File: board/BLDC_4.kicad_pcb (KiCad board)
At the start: 2 copper layers, 100 x 80 mm, 53 parts, among them IC1 MAX3051, P1 Interface, P2 SWD, P3 USB_B, P4 Power, U1 STM32F40X_LQFP64, U2 AP1117D33, X2 8MHz 10ppm

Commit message: - preliminary layout for CPU board ready
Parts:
- removed C23: 1n, Capacitors_SMD:C_0805
- removed C35: 2.2u, Capacitors_SMD:C_0805
- C14: value 2.2u -> 100n
- C18: value 2u2 -> 1n
- moved REF** 390.6 mm to (176.0, 92.0)
- moved C31 106.0 mm to (252.6, 51.4), turned to 90 degrees
- moved C14 105.3 mm to (262.2, 60.0), turned to 180 degrees
- moved C13 83.2 mm to (234.4, 42.8), turned to 225 degrees
- moved C32 77.9 mm to (233.8, 64.2)
- moved C11 72.6 mm to (235.0, 57.0), turned to 180 degrees
- moved C10 68.9 mm to (216.4, 58.8)
- moved C12 66.7 mm to (219.6, 43.2), turned to 270 degrees
- moved C2 44.6 mm to (204.8, 49.2), turned to 180 degrees
- moved C1 30.7 mm to (200.6, 46.0), turned to 270 degrees
- moved C8 14.3 mm to (262.2, 62.0), turned to 0 degrees
- moved C19 10.6 mm to (262.2, 44.0)
- moved C20 8.40 mm to (262.2, 52.4)
- moved C21 5.40 mm to (258.8, 48.2), turned to 90 degrees
- moved C18 5.20 mm to (262.2, 54.8)
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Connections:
- C14 pad 1: GND -> /MCU/ADC_TEMP
- C14 pad 2: +3V3 -> GND
- C18 pad 1: /MCU/ADC_TEMP -> /MCU/BR_SO2
- C19 pad 1: /MCU/BR_SO2 -> /MCU/BR_SO1
- C20 pad 1: /MCU/BR_SO1 -> /MCU/SENS3
- C21 pad 1: /MCU/SENS3 -> /MCU/SENS2
- C22 pad 1: /MCU/SENS2 -> /MCU/SENS1
- P1 pad 18: Net-(P1-Pad18) -> (no net)
- P1 pad 19: Net-(P1-Pad19) -> (no net)
- P1 pad 20: Net-(P1-Pad20) -> (no net)
- P2 pad 6: Net-(P2-Pad6) -> (no net)
- P4 pad 30: Net-(P4-Pad30) -> (no net)
- P4 pad 32: Net-(P4-Pad32) -> (no net)
- P4 pad 34: Net-(P4-Pad34) -> (no net)
- P4 pad 36: Net-(P4-Pad36) -> (no net)
- P4 pad 40: +12V -> (no net)
- U1 pad 11: Net-(U1-Pad11) -> (no net)
- U1 pad 2: Net-(U1-Pad2) -> (no net)
- U1 pad 28: Net-(U1-Pad28) -> (no net)
- U1 pad 3: Net-(U1-Pad3) -> (no net)
- U1 pad 33: /MCU/DC_CAL -> (no net)
- U1 pad 39: Net-(U1-Pad39) -> (no net)
- U1 pad 4: Net-(U1-Pad4) -> (no net)
- U1 pad 40: Net-(U1-Pad40) -> (no net)
- U1 pad 50: Net-(U1-Pad50) -> (no net)
- U1 pad 53: /MCU/FAULT -> (no net)
- U1 pad 54: Net-(U1-Pad54) -> (no net)
- U1 pad 55: Net-(U1-Pad55) -> (no net)
- U1 pad 56: Net-(U1-Pad56) -> (no net)
- U1 pad 9: Net-(U1-Pad9) -> (no net)
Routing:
- net +3V3: track 14.8 -> 231.1 mm, vias 0 -> 5
- net GND: track 0.00 -> 47.9 mm, vias 0 -> 5
- net SWDIO: track 19.9 -> 25.6 mm
- net /MCU/AN_IN: track 46.9 -> 51.6 mm
- net /Filters/HALL2_OUT: track 66.5 -> 71.0 mm
- net /Filters/HALL1_OUT: track 56.1 -> 60.1 mm
- net Net-(P1-Pad16): track 6.45 -> 10.2 mm
- net /Filters/HALL3_OUT: track 61.3 -> 64.8 mm
- net NRST: track 48.1 -> 46.6 mm
- net /MCU/SERVO: track 111.5 -> 110.2 mm
- net /MCU/EN_GATE: track 92.0 -> 93.1 mm
- net Net-(C1-Pad1): track 25.0 -> 26.0 mm
- net /CAN bus transceiver/CAN_TX: track 122.9 -> 123.6 mm
- net Net-(C17-Pad1): track 2.96 -> 3.62 mm
- added copper zone on B.Cu, net GND
- added copper zone on F.Cu, net GND

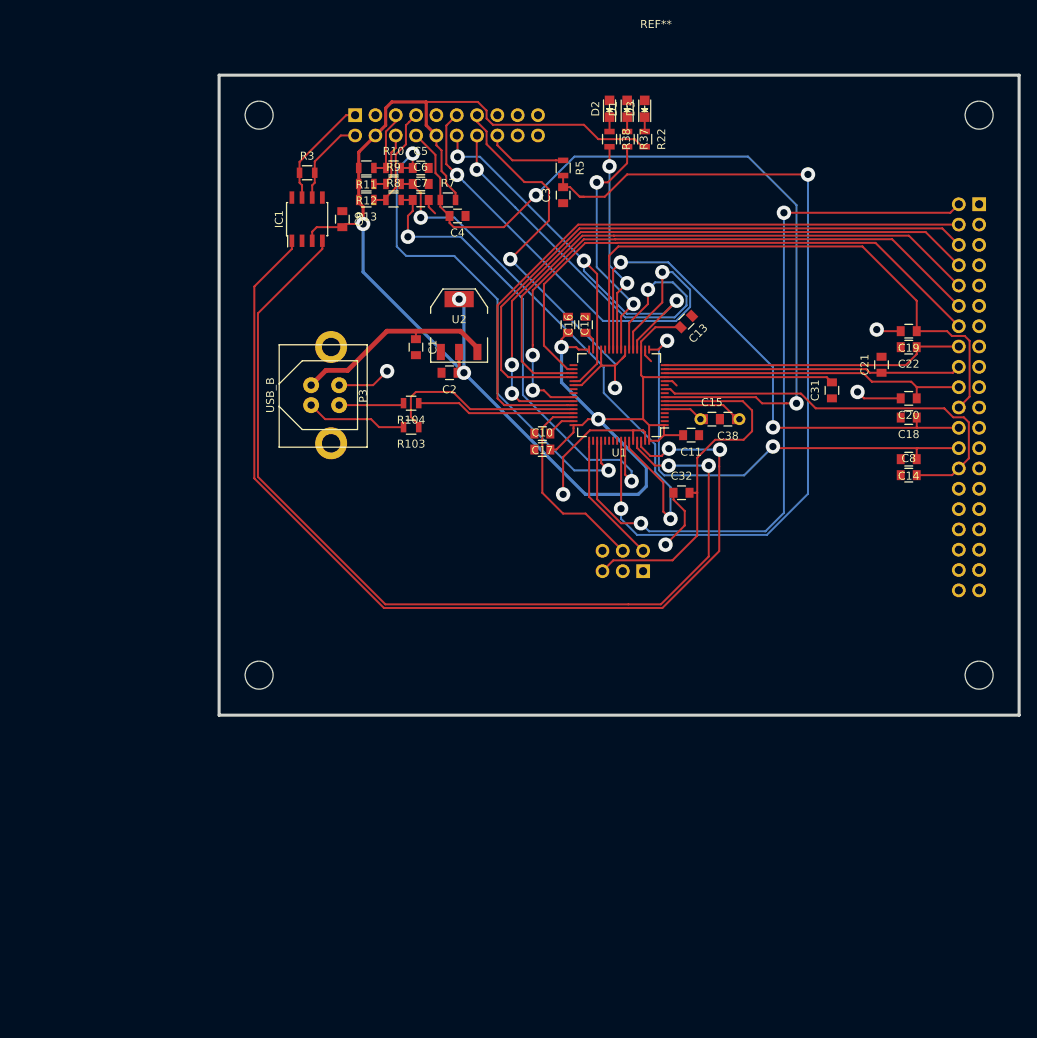
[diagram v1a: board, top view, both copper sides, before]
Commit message: - updated layout with recent changes in schematic
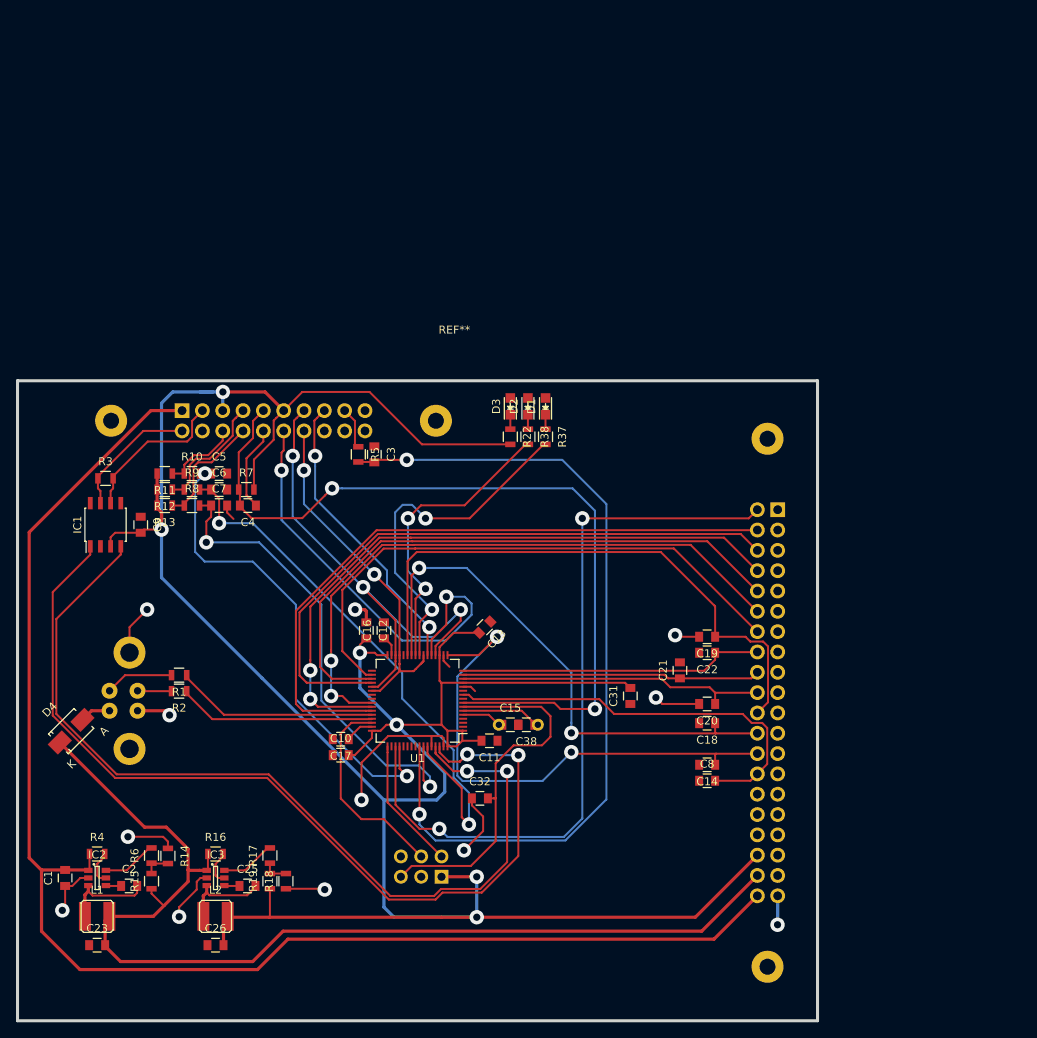
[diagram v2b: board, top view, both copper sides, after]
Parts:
- removed R103, R104: 22R, Resistors_SMD:R_0805
- removed the REF** at (176.0, 92.0)
- removed U2: AP1117D33, TO_SOT_Packages_SMD:SOT-223
- added C23: 22u, Capacitors_SMD:C_0805, F.Cu at (160.8, 120.8)
- added C25: 1u, Capacitors_SMD:C_0805, F.Cu at (179.6, 113.3)
- added C26: 22u, Capacitors_SMD:C_0805, F.Cu at (175.6, 120.8)
- added D4: SS14, Diodes_SMD:SMA_Standard, F.Cu at (157.5, 94.0)
- added IC2: AP65101, TO_SOT_Packages_SMD:SOT-23-6, F.Cu at (160.8, 112.3)
- added IC3: AP65101, TO_SOT_Packages_SMD:SOT-23-6, F.Cu at (175.6, 112.3)
- added L1: 6u8, alexmod:SRN4026, F.Cu at (160.8, 117.2)
- added L2: 6u8, alexmod:SRN4026, F.Cu at (175.6, 117.2)
- added R1: 22R, Resistors_SMD:R_0805, F.Cu at (171.0, 87.0)
- added R14: 7k68, Resistors_SMD:R_0805, F.Cu at (169.6, 109.6)
- added R15: 40k2, Resistors_SMD:R_0805, F.Cu at (167.6, 112.8)
- added R16: 100k, Resistors_SMD:R_0805, F.Cu at (175.6, 109.3)
- added R17: 59k, Resistors_SMD:R_0805, F.Cu at (182.3, 109.5)
- added R18: 13k, Resistors_SMD:R_0805, F.Cu at (184.3, 112.8)
- added R19: 40k2, Resistors_SMD:R_0805, F.Cu at (182.3, 112.8)
- added R2: 22R, Resistors_SMD:R_0805, F.Cu at (171.0, 89.0)
- added R4: 100k, Resistors_SMD:R_0805, F.Cu at (160.8, 109.3)
- added R6: 59k, Resistors_SMD:R_0805, F.Cu at (167.6, 109.5)
- added REF**: EuroBoard_halb_Type-I_100mmX80mm, EuroBoard_Outline:EuroBoard_halb_Type-I_100mmX80mm, F.Cu at (150.8, 130.2)
- C1: value 100n -> 22u
- C2: value 100n -> 1u
- P1: footprint Pin_Headers:Pin_Header_Straight_2x10 -> alexmod:XG4A_20
- P3: moved to B.Cu
- P4: footprint Pin_Headers:Pin_Header_Straight_2x20 -> alexmod:XG4A_40
- moved C1 79.5 mm to (156.8, 112.3), turned to 90 degrees
- moved C2 75.6 mm to (164.8, 113.3), turned to 0 degrees
- moved P4 67.7 mm to (244.6, 90.5), turned to 270 degrees
- moved C10 45.8 mm to (191.2, 97.0)
- moved C13 45.8 mm to (209.2, 81.0)
- moved C16 45.8 mm to (196.6, 81.4)
- moved C17 45.8 mm to (191.2, 95.0)
- moved C21 45.8 mm to (233.6, 86.4)
- moved C32 45.8 mm to (208.6, 102.4)
- moved C9 45.8 mm to (166.2, 68.2)
- moved R10 45.8 mm to (172.6, 61.8)
- moved R11 45.8 mm to (169.2, 61.8)
- moved R12 45.8 mm to (169.2, 63.8)
- moved R13 45.8 mm to (169.2, 65.8)
- moved R8 45.8 mm to (172.6, 65.8)
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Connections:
- C1 pad 1: Net-(C1-Pad1) -> GND
- C1 pad 2: GND -> +12V
- C2 pad 1: +3V3 -> Net-(C2-Pad1)
- C2 pad 2: GND -> Net-(C2-Pad2)
- P1 pad 1: /CAN bus transceiver/CANH -> +12V
- P1 pad 10: +3V3 -> GND
- P1 pad 11: /MCU/SCK_ADC_EXT -> +3V3
- P1 pad 12: /MCU/TX_SDA_NSS -> /MCU/SCK_ADC_EXT
- P1 pad 13: /MCU/RX_SCL_MOSI -> /MCU/TX_SDA_NSS
- P1 pad 14: /MCU/MISO_ADC_EXT2 -> /MCU/RX_SCL_MOSI
- P1 pad 15: GND -> /MCU/MISO_ADC_EXT2
- P1 pad 16: Net-(P1-Pad16) -> GND
- P1 pad 17: GND -> Net-(P1-Pad17)
- P1 pad 18: (no net) -> GND
- P1 pad 2: /CAN bus transceiver/CANL -> /CAN bus transceiver/CANH
- P1 pad 3: GND -> /CAN bus transceiver/CANL
- P1 pad 4: +3V3 -> GND
- P1 pad 5: /Filters/HALL3_IN -> +3V3
- P1 pad 6: /Filters/HALL2_IN -> /Filters/HALL3_IN
- P1 pad 7: /Filters/HALL1_IN -> /Filters/HALL2_IN
- P1 pad 8: /Filters/TEMP_IN -> /Filters/HALL1_IN
- P1 pad 9: GND -> /Filters/TEMP_IN
- P3 pad 1: Net-(C1-Pad1) -> Net-(D4-Pad2)
- P4 pad 36: (no net) -> +3V3
- P4 pad 38: +3V3 -> +5V
- P4 pad 40: (no net) -> +12V
- R5 pad 1: Net-(P1-Pad16) -> Net-(P1-Pad17)
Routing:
- net +12V: track 0.00 -> 179.2 mm
- net +5V: track 0.00 -> 135.3 mm
- net +3V3: track 231.1 -> 352.0 mm, vias 5 -> 6
- net GND: track 47.9 -> 93.1 mm, vias 5 -> 12
- net Net-(C1-Pad1): track 26.0 -> 0.00 mm
- net /MCU/MISO_ADC_EXT2: track 54.3 -> 37.1 mm
- net /MCU/RX_SCL_MOSI: track 60.4 -> 44.1 mm
- net /MCU/LED_GREEN: track 30.3 -> 44.1 mm
- net Net-(C2-Pad2): track 0.00 -> 11.4 mm
- net Net-(C25-Pad2): track 0.00 -> 10.8 mm
- net /MCU/LED_RED: track 26.8 -> 37.4 mm
- net Net-(P1-Pad16): track 10.2 -> 0.00 mm
- net /CAN bus transceiver/CANL: track 11.0 -> 19.2 mm
- net /MCU/SCK_ADC_EXT: track 63.7 -> 55.6 mm
- net /Filters/HALL2_IN: track 8.37 -> 16.0 mm
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
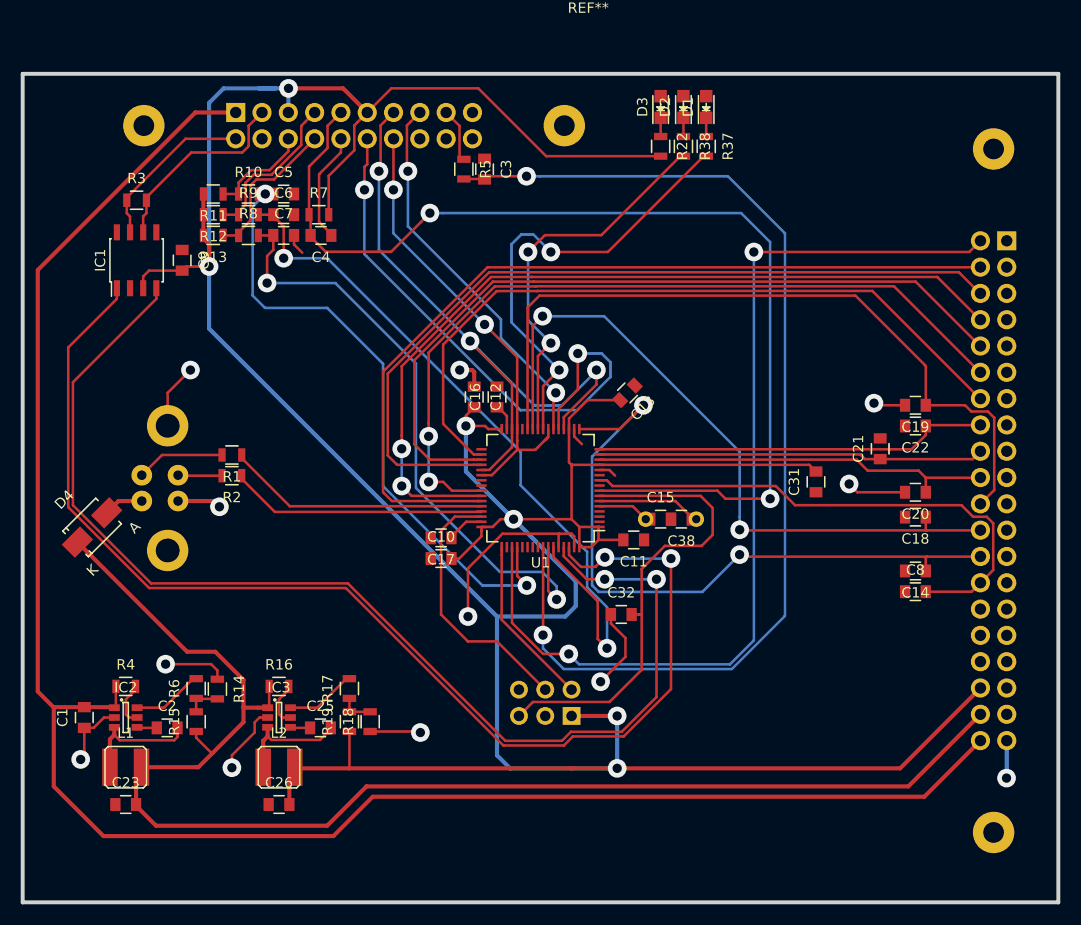
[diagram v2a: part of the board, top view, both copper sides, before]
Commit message: - CAN interface isolation
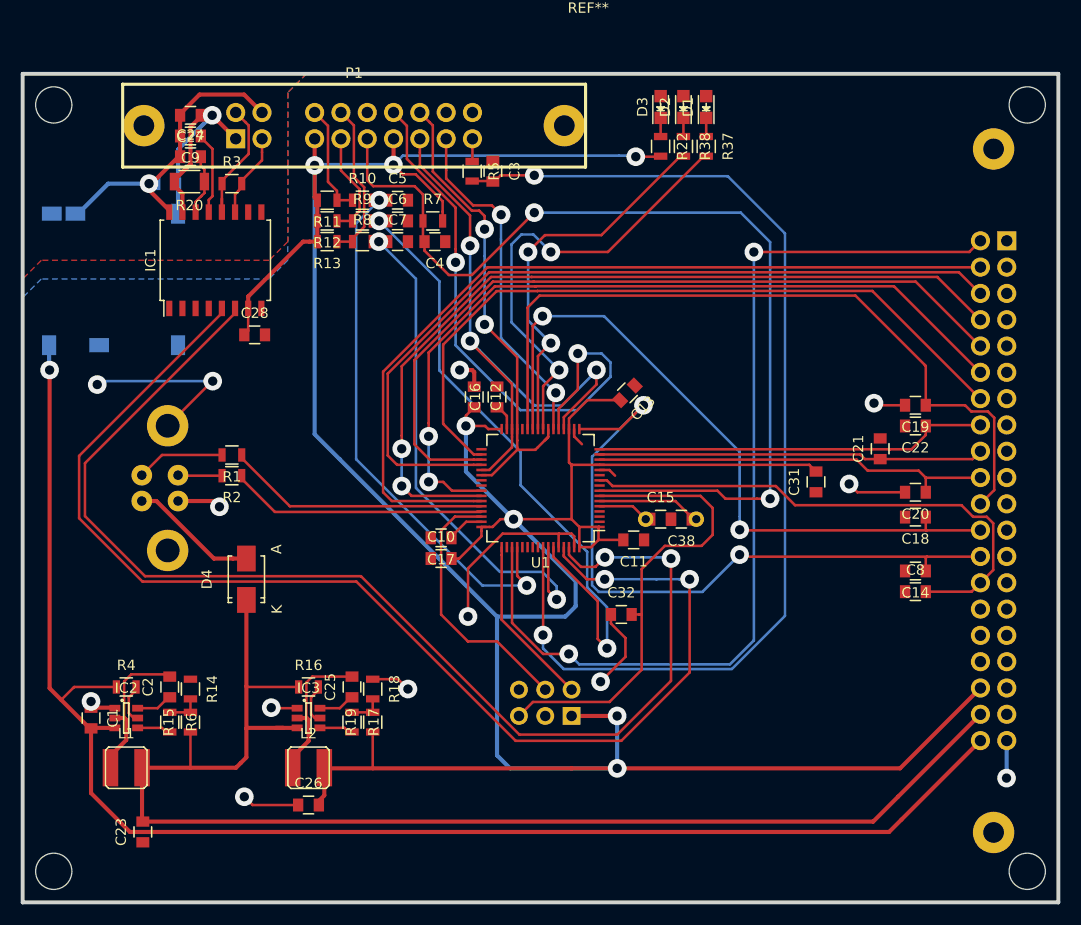
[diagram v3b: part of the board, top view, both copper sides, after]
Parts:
- removed the REF** at (150.8, 130.2)
- added B1: MTC1, alexmod:MTC1, B.Cu at (159.6, 70.0)
- added C24: 22u, Capacitors_SMD:C_0805, F.Cu at (167.0, 58.2)
- added C27: 100n, Capacitors_SMD:C_0805, F.Cu at (167.0, 54.2)
- added C28: 100n, Capacitors_SMD:C_0805, F.Cu at (173.2, 75.4)
- added C29: 22u, Capacitors_SMD:C_0805, B.Cu at (164.6, 60.8)
- added R20: 300R, Resistors_SMD:R_1206, F.Cu at (166.9, 60.6)
- added REF**: EuroBoard_halb_Type-I_100mmX80mm_holes, EuroBoard_Outline:EuroBoard_halb_Type-I_100mmX80mm_holes, F.Cu at (150.8, 130.2)
- C10, C11, C12, C13, C16, C17, C31: value 2.2u -> 1u
- C9: value 100n -> 1u
- IC1: value MAX3051 -> ADM3052; footprint Housings_SOIC:SOIC-8_3.9x4.9mm_Pitch1.27mm -> Housings_SOIC:SOIC-16_7.5x10.3mm_Pitch1.27mm
- IC2, IC3: value AP65101 -> AP65201
- P1: value Interface -> CONN_01X18_20; footprint alexmod:XG4A_20 -> alexmod:XG4A_20_wo_56; moved to F.Cu
- R17, R6: value 59k -> 75k
- R37, R38: value 100R -> 120R
- moved D4 15.7 mm to (172.4, 99.0), turned to 90 degrees
- moved C9 12.0 mm to (167.0, 56.2), turned to 180 degrees
- moved C4 11.0 mm to (190.6, 66.4)
- moved C5 11.0 mm to (187.0, 62.4)
- moved C6 11.0 mm to (187.0, 64.4)
- moved C7 11.0 mm to (187.0, 66.4)
- moved R10 11.0 mm to (183.6, 62.4)
- moved R11 11.0 mm to (180.2, 62.4)
- moved R12 11.0 mm to (180.2, 64.4)
- moved R13 11.0 mm to (180.2, 66.4)
- moved R7 11.0 mm to (190.4, 64.4)
- moved R8 11.0 mm to (183.6, 66.4)
- moved R9 11.0 mm to (183.6, 64.4)
- moved R3 9.34 mm to (171.0, 60.8)
- moved IC1 7.60 mm to (169.4, 68.2)
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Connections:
- C9 pad 1: GND -> Net-(C9-Pad1)
- C9 pad 2: +3V3 -> Earth
- IC1 pad 1: /CAN bus transceiver/CAN_TX -> (no net)
- IC1 pad 3: +3V3 -> GND
- IC1 pad 4: /CAN bus transceiver/CAN_RX -> (no net)
- IC1 pad 5: GND -> /CAN bus transceiver/CAN_RX
- IC1 pad 6: /CAN bus transceiver/CANL -> /CAN bus transceiver/CAN_TX
- IC1 pad 7: /CAN bus transceiver/CANH -> +3V3
- IC2 pad 1: +12V -> GND
- IC2 pad 2: GND -> Net-(C2-Pad2)
- IC2 pad 3: Net-(C2-Pad2) -> +12V
- IC2 pad 4: Net-(C2-Pad1) -> Net-(IC2-Pad4)
- IC2 pad 6: Net-(IC2-Pad6) -> Net-(C2-Pad1)
- IC3 pad 1: +5V -> GND
- IC3 pad 2: GND -> Net-(C25-Pad2)
- IC3 pad 3: Net-(C25-Pad2) -> +5V
- IC3 pad 4: Net-(C25-Pad1) -> Net-(IC3-Pad4)
- IC3 pad 6: Net-(IC3-Pad6) -> Net-(C25-Pad1)
- P1 pad 1: +12V -> +12VA
- P1 pad 10: GND -> /Filters/HALL1_IN
- P1 pad 11: +3V3 -> /Filters/TEMP_IN
- P1 pad 12: /MCU/SCK_ADC_EXT -> GND
- P1 pad 13: /MCU/TX_SDA_NSS -> +3V3
- P1 pad 14: /MCU/RX_SCL_MOSI -> /MCU/SCK_ADC_EXT
- P1 pad 15: /MCU/MISO_ADC_EXT2 -> /MCU/TX_SDA_NSS
- P1 pad 16: GND -> /MCU/RX_SCL_MOSI
- P1 pad 17: Net-(P1-Pad17) -> /MCU/MISO_ADC_EXT2
- P1 pad 19: (no net) -> Net-(P1-Pad19)
- P1 pad 20: (no net) -> GND
- P1 pad 4: GND -> Earth
- P1 pad 7: /Filters/HALL2_IN -> +3V3
- P1 pad 8: /Filters/HALL1_IN -> /Filters/HALL3_IN
- P1 pad 9: /Filters/TEMP_IN -> /Filters/HALL2_IN
- R17 pad 2: Net-(IC3-Pad6) -> Net-(IC3-Pad4)
- R5 pad 1: Net-(P1-Pad17) -> Net-(P1-Pad19)
- R6 pad 2: Net-(IC2-Pad6) -> Net-(IC2-Pad4)
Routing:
- net +12V: track 179.2 -> 144.3 mm, vias 0 -> 1
- net Earth: track 0.00 -> 30.7 mm, vias 0 -> 1
- net +12VA: track 0.00 -> 26.3 mm, vias 0 -> 1
- net +3V3: track 352.0 -> 327.3 mm, vias 6 -> 7
- net /CAN bus transceiver/CANL: track 19.2 -> 8.16 mm
- net GND: track 93.1 -> 82.2 mm, vias 12 -> 13
- net /Filters/HALL1_OUT: track 60.1 -> 50.9 mm
- net Net-(C9-Pad1): track 0.00 -> 8.42 mm
- net Net-(D4-Pad2): track 4.11 -> 12.4 mm
- net /Filters/HALL3_OUT: track 60.8 -> 53.0 mm
- net /Filters/TEMP_IN: track 102.6 -> 95.4 mm
- net /Filters/HALL2_OUT: track 71.0 -> 63.9 mm
- net Net-(IC2-Pad6): track 6.86 -> 0.00 mm
- net Net-(IC3-Pad6): track 6.86 -> 0.00 mm
- net Net-(C24-Pad2): track 0.00 -> 5.85 mm
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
